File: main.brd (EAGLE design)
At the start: 60.6 x 25.4 mm, 6 parts

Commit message: Fix unused tracks, added R values.
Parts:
- R1, R2: value (none) -> 10k
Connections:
- net N$3: no longer S2_PROG.3
- net N$7: no longer S1_RESET.2
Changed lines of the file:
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@@
 <attribute name="MF" value="" x="20.32" y="67.31" size="1.778" layer="27" rot="R90" display="off"/>
 </element>
-<element name="R1" library="resistor" package="0204/7" value="" x="45.72" y="64.77" rot="R270"/>
-<element name="R2" library="resistor" package="0204/7" value="" x="43.18" y="64.77" rot="R270"/>
+<element name="R1" library="resistor" package="0204/7" value="10k" x="45.72" y="64.77" rot="R270"/>
+<element name="R2" library="resistor" package="0204/7" value="10k" x="43.18" y="64.77" rot="R270"/>
 <element name="S1_RESET" library="switch-omron" package="B3F-10XX" value="" x="35.56" y="62.23" rot="R270">
 <attribute name="MPN" value="B3F-1000" x="35.56" y="62.23" size="1.778" layer="27" rot="R270" display="off"/>
@@
 <signal name="N$3">
 <contactref element="ESP8266_TO_PROG" pad="GPIO0"/>
-<contactref element="S2_PROG" pad="3"/>
 <contactref element="S2_PROG" pad="4"/>
 <wire x1="37.8206" y1="75.6412" x2="52.6288" y2="75.6412" width="0.4064" layer="16"/>
@@
 <wire x1="57.15" y1="71.12" x2="57.15" y2="67.8825" width="0.4064" layer="16"/>
 <wire x1="57.15" y1="67.8825" x2="55.3225" y2="66.055" width="0.4064" layer="16" curve="-90"/>
-<wire x1="37.8206" y1="69.1388" x2="37.8206" y2="75.6412" width="0" layer="19" extent="1-1"/>
 </signal>
 <signal name="N$6">
@@
 <contactref element="R2" pad="1"/>
 <contactref element="S1_RESET" pad="1"/>
-<contactref element="S1_RESET" pad="2"/>
 <wire x1="43.18" y1="68.58" x2="43.18" y2="66.04" width="0.4064" layer="16"/>
 <wire x1="43.18" y1="66.04" x2="38.1" y2="66.04" width="0.4064" layer="16"/>
@@
 <wire x1="38.1" y1="65.7606" x2="37.8206" y2="65.4812" width="0.4064" layer="16"/>
 <wire x1="52.7825" y1="66.055" x2="43.18" y2="66.04" width="0.4064" layer="16"/>
-<wire x1="37.8206" y1="58.9788" x2="37.8206" y2="65.4812" width="0" layer="19" extent="1-1"/>
 </signal>
 </signals>

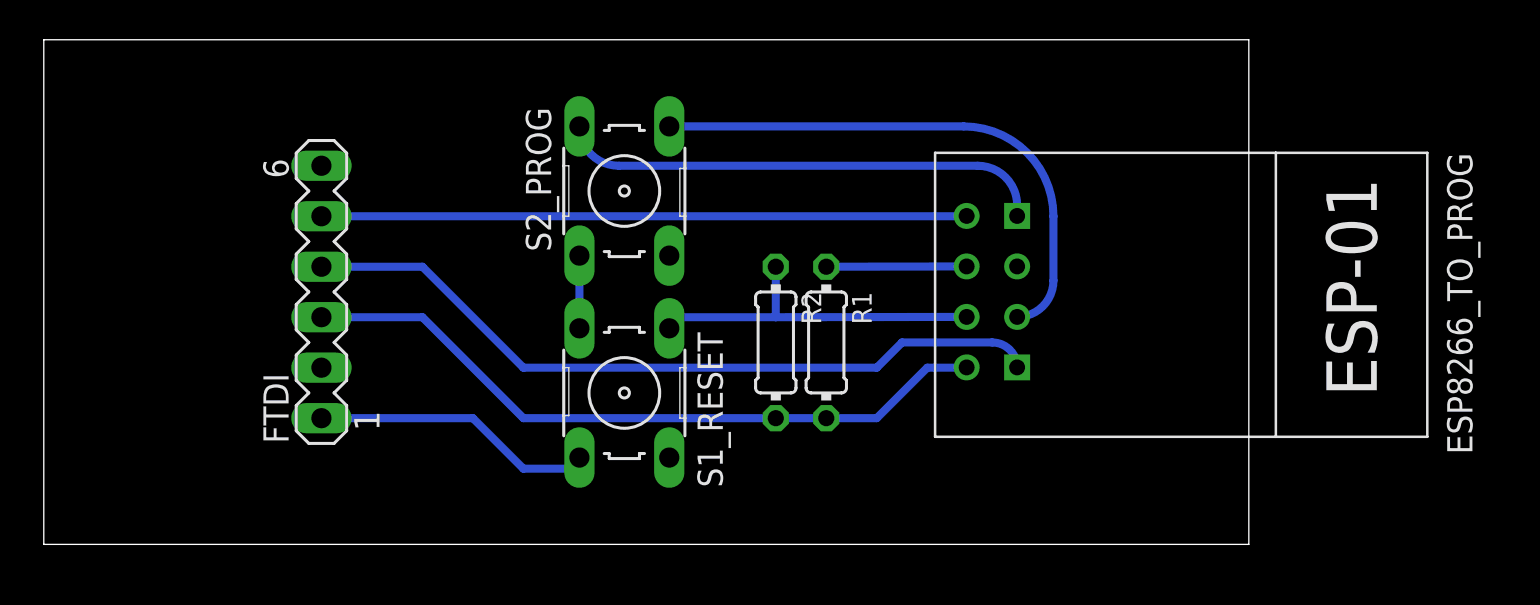
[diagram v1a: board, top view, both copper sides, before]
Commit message: Board: FTDI placement, use 45 degrees corners, added text.
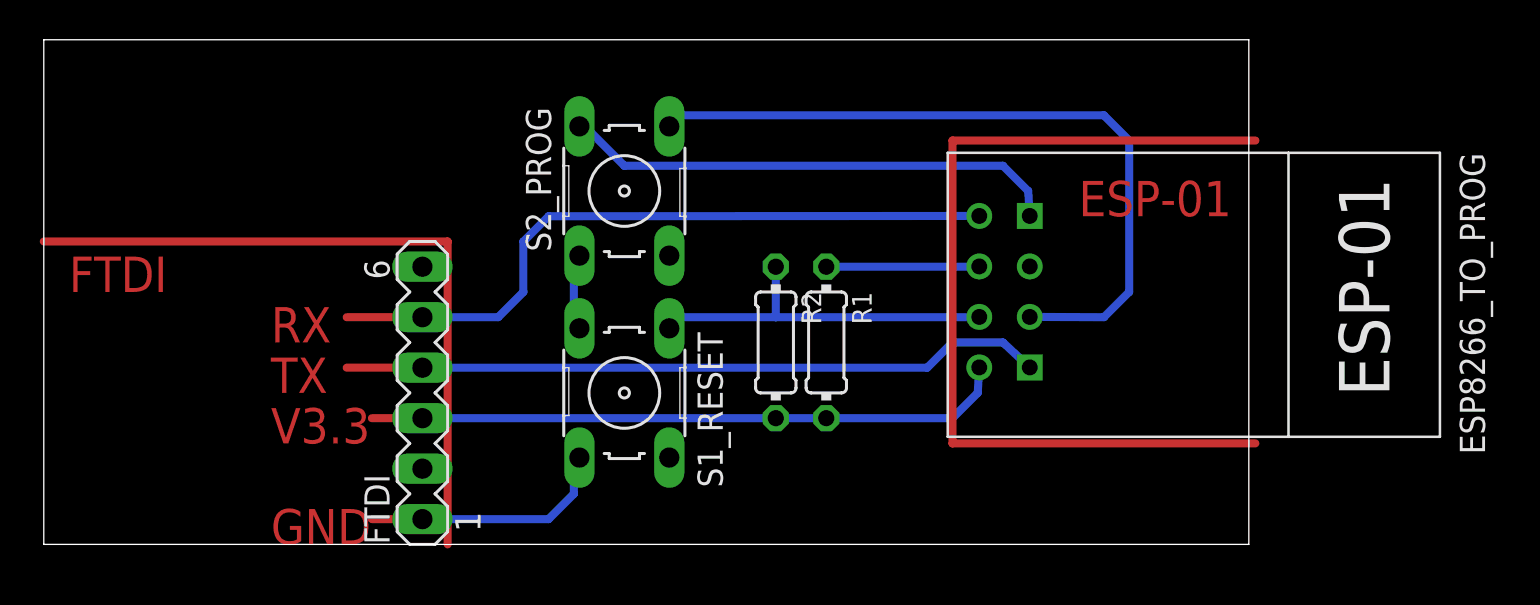
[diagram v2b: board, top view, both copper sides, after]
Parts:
- moved FTDI 7.18 mm to (25.4, 62.2)
- moved ESP8266_TO_PROG 0.63 mm to (61.6, 67.3)
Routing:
- net N$10: track 0.00 -> 45.7 mm
- net N$1: track 0.00 -> 35.6 mm
- net N$3: track 27.0 -> 37.2 mm
- net TX: track 38.2 -> 31.6 mm
- net V3.3: track 35.6 -> 29.8 mm
- net N$5: track 0.00 -> 2.54 mm
- net N$4: track 0.00 -> 2.54 mm
- net N$9: track 0.00 -> 1.27 mm
- net N$8: track 0.00 -> 1.27 mm
- net RX: track 32.5 -> 31.6 mm
- net GND: track 42.3 -> 41.6 mm
- net N$7: track 17.9 -> 18.5 mm
- net N$6: track 7.06 -> 7.70 mm
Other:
- board text added: "ESP-01"
- board text added: "FTDI"
- board text added: "GND"
- board text added: "RX"
- board text added: "TX"
- board text added: "V3.3"
